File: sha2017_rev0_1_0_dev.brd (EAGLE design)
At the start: 95 x 86 mm, 196 parts, among them IC1 CP210X_USB_UART, IC2 AP7215, IC3 ESP32WROOM32, IC4 MCP73833, IC5 FXL6408, IC6 CPT112, Q1 MOSFET-PCHANNEL, Q2 MMBT2222A, Q3 MMBT2222A, Q4 MMBT2222A, Q5 MMBT2222A, Q6 SI1304 BDL, Q7 MMBT2222A, Q8 MOSFET-PCHANNEL, T1 SI2301DS, X1 2908-05WB-MG, X3 JST-PH3

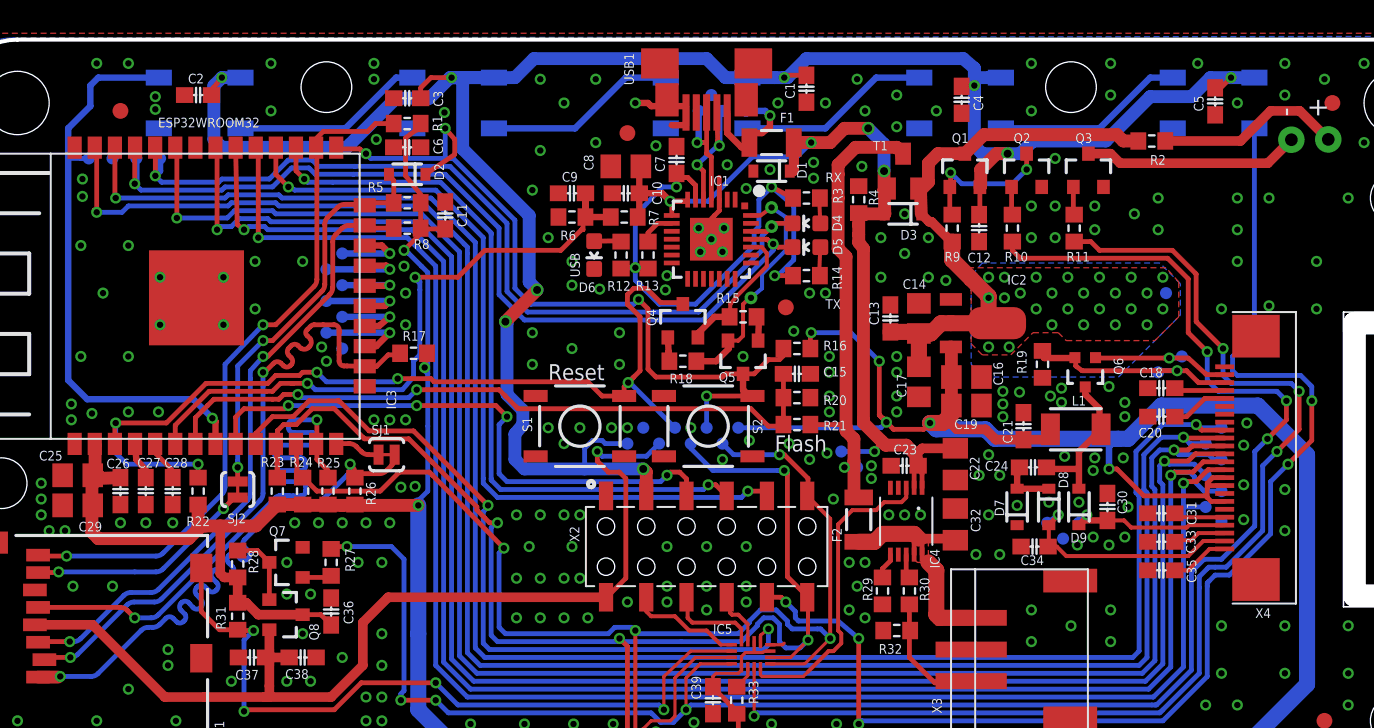
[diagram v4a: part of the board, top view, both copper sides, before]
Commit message: add 1 LED
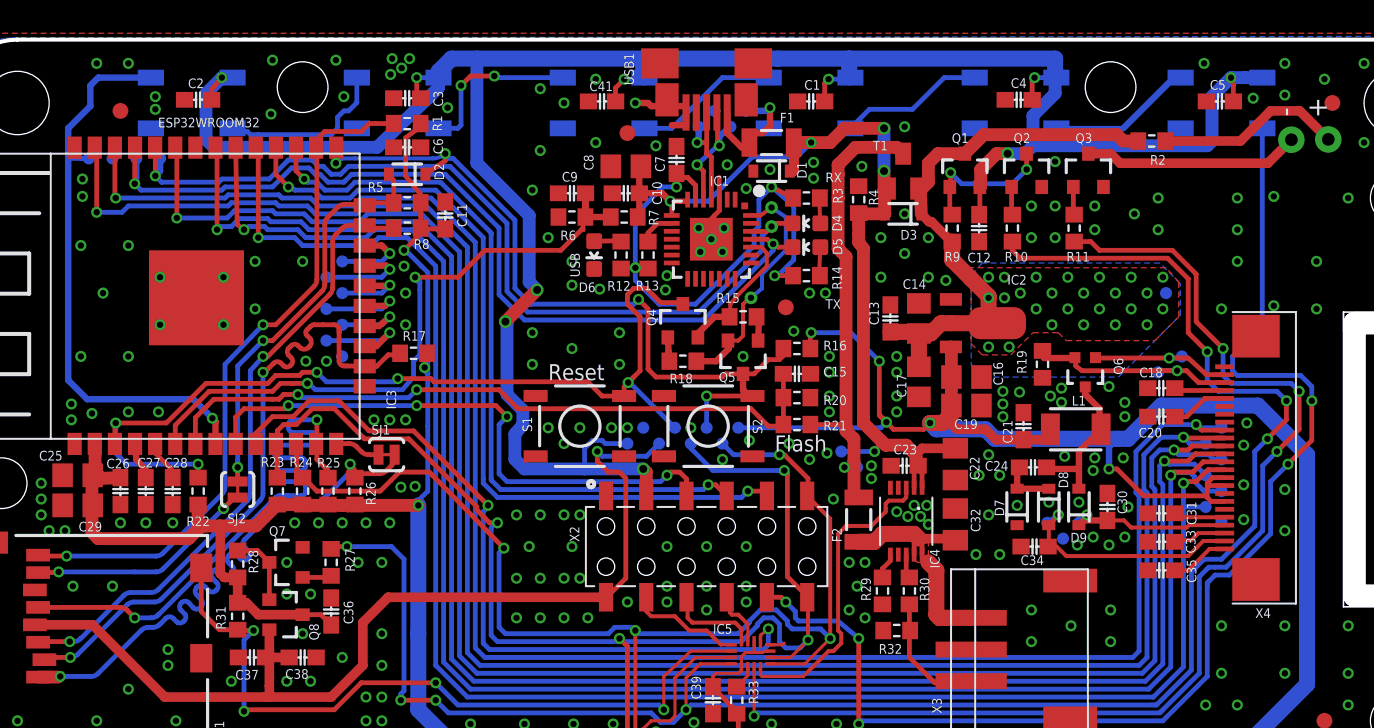
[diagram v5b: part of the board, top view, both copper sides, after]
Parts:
- added C41: 100n, sha2017_rev0_1_0_dev:C0603-DASHES
- added D105: (no value), SparkFun-LED:WS2812B
- moved D103 9.50 mm to (41.0, 81.0)
- moved D102 6.50 mm to (54.0, 81.0)
- moved C4 3.60 mm to (67.2, 81.2), turned to 180 degrees
- moved D101 3.50 mm to (67.0, 81.0)
- moved TP137 1.12 mm to (49.0, 79.5)
- moved TP139 1.02 mm to (48.0, 80.5)
- moved TP138 1.00 mm to (47.0, 79.5)
- moved C1 0.85 mm to (54.1, 81.1), turned to 0 degrees
- moved D100 0.50 mm to (80.0, 81.0)
- moved D104 0.50 mm to (15.0, 81.0)
- moved TP124 0.50 mm to (24.5, 65.0)
- moved TP125 0.50 mm to (23.5, 66.0)
- moved TP126 0.50 mm to (24.5, 67.0)
- moved TP127 0.50 mm to (23.5, 68.0)
- moved TP129 0.50 mm to (24.5, 69.0)
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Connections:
- removed net N$51: D103.4, D104.2
- new net N$3: D103.4, D105.2
- new net N$4: D104.2, D105.4
- net GND: now also C41.1, D105.3
- net WS2812_POWER: now also C41.2, D105.1
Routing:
- net N$51: track 12.2 -> 0.00 mm
- net N$4: track 0.00 -> 10.8 mm
- net N$3: track 0.00 -> 10.8 mm, vias 0 -> 2
- net WS2812_POWER: track 148.5 -> 153.9 mm, vias 9 -> 10
- net N$50: track 12.2 -> 9.17 mm
- net N$2: track 12.2 -> 9.17 mm
- net N$19: track 12.2 -> 9.17 mm
- net ESP32_FLASH: track 53.4 -> 50.6 mm
- net USB_DP_CON: track 8.30 -> 7.30 mm
- net USB_DN_CON: track 8.68 -> 7.87 mm
- net +5V: track 64.1 -> 64.7 mm
- net GND: vias 286 -> 282

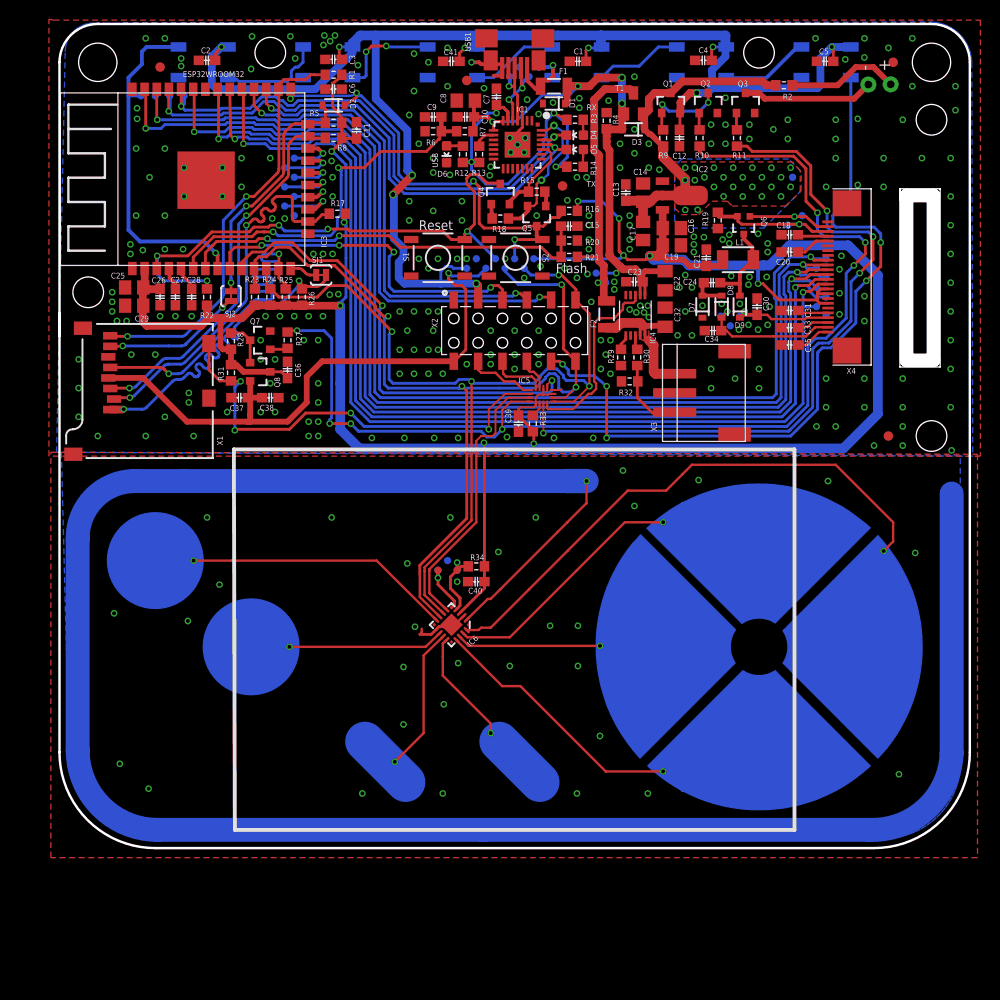
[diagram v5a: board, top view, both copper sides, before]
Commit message: adjusted values and add moe coper to the charger region
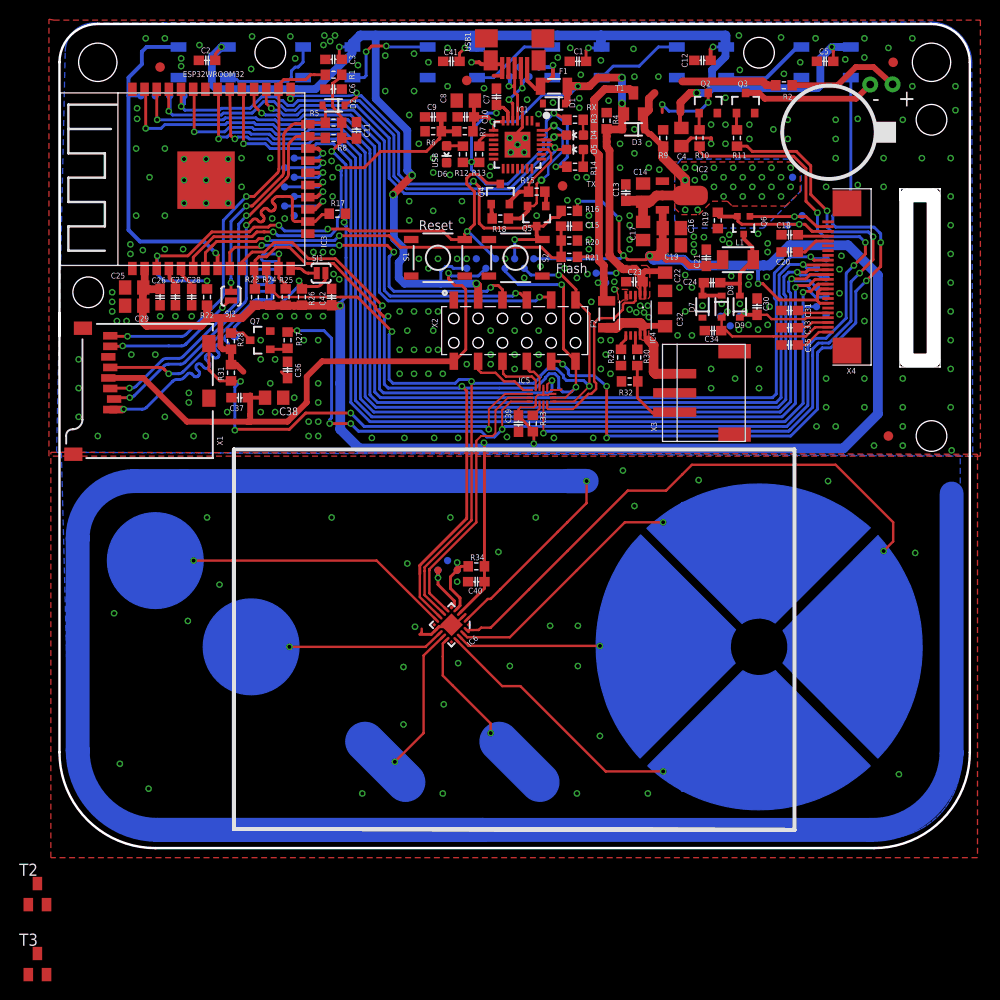
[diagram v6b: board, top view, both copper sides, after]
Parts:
- removed Q1, Q8: MOSFET-PCHANNEL, SparkFun-DiscreteSemi:SOT23-3
- added C42: 100n, sha2017_rev0_1_0_dev:C0603-DASHES
- added T2, T3: SI2301DS, transistor-small-signal:SOT23
- C22, C32: value 10u -> 4u7/16V; device rcl:C0805K -> rcl:C0805
- C38, C4: device 00ralf:C0603-DASHES -> rcl:C0805
- C39: value (none) -> 100n
- D100, D101, D102, D103, D104, D105: value (none) -> SK6812
- R2: value 10R -> 27R
- SJ1, SJ2: value JUMPER-PAD-2-NC_BY_TRACE -> JUMPER-PAD-2-NOYES_SILK; device SparkFun-Passives:PAD-JUMPER-2-NC_BY_TRACE_YES_SILK -> SparkFun-Passives:PAD-JUMPER-2-NO_YES_SILK
- moved C12 8.45 mm to (67.1, 81.2), turned to 0 degrees
- moved C4 8.32 mm to (64.9, 73.2), turned to 270 degrees
- moved C38 0.40 mm to (22.4, 46.0)
- moved SJ1 0.20 mm to (27.3, 59.0)
- moved U$1 0.20 mm to (80.5, 73.7)
- moved C22 0.10 mm to (63.2, 58.1), turned to 270 degrees
- turned C32 to 90 degrees
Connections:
- net +3V3: now also C42.1; no longer Q8.3
- net +5V: now also C22.1; no longer C22.2
- net 3V3_SWITCHED: no longer Q8.2
- net GND: now also C22.2, C32.2, C42.2; no longer C22.1, C32.1
- net N$17: now also T3.1; no longer Q8.1
- net N$49: now also C32.1; no longer C32.2
- net N$53: now also T2.1; no longer Q1.1
- net VCC: no longer Q1.3
- net WS2812_POWER: no longer Q1.2
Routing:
- net PROXIMITY: track 224.4 -> 258.4 mm
- net GND: track 15.0 -> 19.1 mm, vias 282 -> 301
- net +3V3: track 269.8 -> 266.3 mm
- net VCC: track 38.3 -> 34.9 mm
- net N$17: track 4.66 -> 2.31 mm
- net N$53: track 9.20 -> 7.52 mm
- net 3V3_SWITCHED: track 63.9 -> 62.8 mm
- net I2C_SCL: track 95.3 -> 94.3 mm
- net WS2812_POWER: track 153.9 -> 154.4 mm
- added copper zone on layer 1, net +5V
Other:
- board text added: "+"
- board text added: "-"

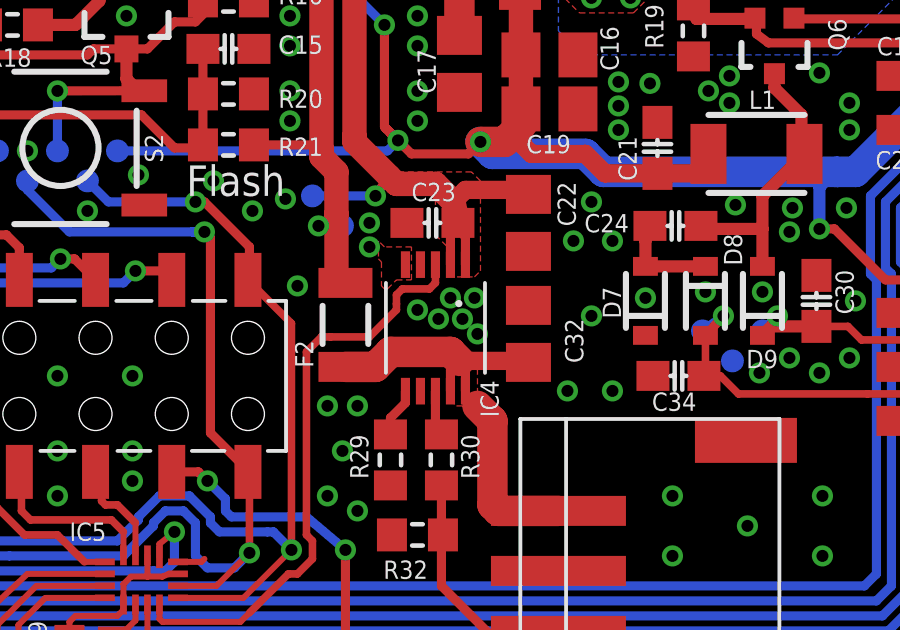
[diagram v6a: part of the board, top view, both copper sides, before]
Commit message: MOOOOOOOORRRRREEEEEEE VIAS for the charger
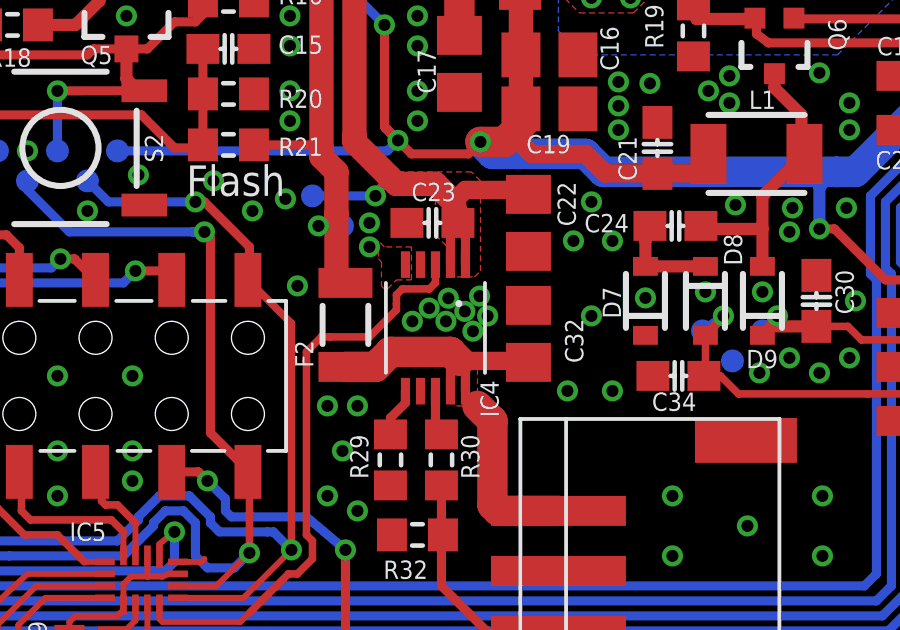
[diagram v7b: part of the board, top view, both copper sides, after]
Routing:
- net GND: vias 301 -> 303
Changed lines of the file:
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@@
 <setting verticaltext="up"/>
 </settings>
-<grid distance="0.1" unitdist="mm" unit="mm" style="lines" multiple="1" display="yes" altdistance="0.025" altunitdist="inch" altunit="inch"/>
+<grid distance="0.01" unitdist="mm" unit="mm" style="lines" multiple="1" display="yes" altdistance="0.025" altunitdist="inch" altunit="inch"/>
 <layers>
 <layer number="1" name="Top" color="4" fill="1" visible="yes" active="yes"/>
@@
 <via x="64.5" y="52.5" extent="1-16" drill="0.4"/>
 <via x="66" y="52.5" extent="1-16" drill="0.4"/>
-<via x="59.5" y="55.2" extent="1-16" drill="0.4"/>
-<via x="60.2" y="54.9" extent="1-16" drill="0.4"/>
-<via x="61" y="54.9" extent="1-16" drill="0.4"/>
+<via x="59.89" y="55.26" extent="1-16" drill="0.4"/>
+<via x="60.45" y="54.82" extent="1-16" drill="0.4"/>
+<via x="61.08" y="55.15" extent="1-16" drill="0.4"/>
 <via x="57.5" y="52" extent="1-16" drill="0.4"/>
 <via x="56.5" y="52" extent="1-16" drill="0.4"/>
@@
 <via x="81.4" y="56.9" extent="1-16" drill="0.4"/>
 <via x="81.4" y="59.4" extent="1-16" drill="0.4"/>
-<via x="60.6" y="55.6" extent="1-16" drill="0.4"/>
-<via x="61.4" y="55.6" extent="1-16" drill="0.4"/>
-<via x="61.5" y="54.4" extent="1-16" drill="0.4"/>
+<via x="60.53" y="55.59" extent="1-16" drill="0.4"/>
+<via x="61.57" y="55.66" extent="1-16" drill="0.4"/>
+<via x="61.84" y="55" extent="1-16" drill="0.4"/>
 <contactref element="D105" pad="3"/>
 <contactref element="C41" pad="1"/>
@@
 <vertex x="58.3" y="56"/>
 </polygon>
+<via x="59.33" y="54.82" extent="1-16" drill="0.4"/>
+<via x="61.35" y="54.49" extent="1-16" drill="0.4"/>
 </signal>
 <signal name="USB_DN_CON">

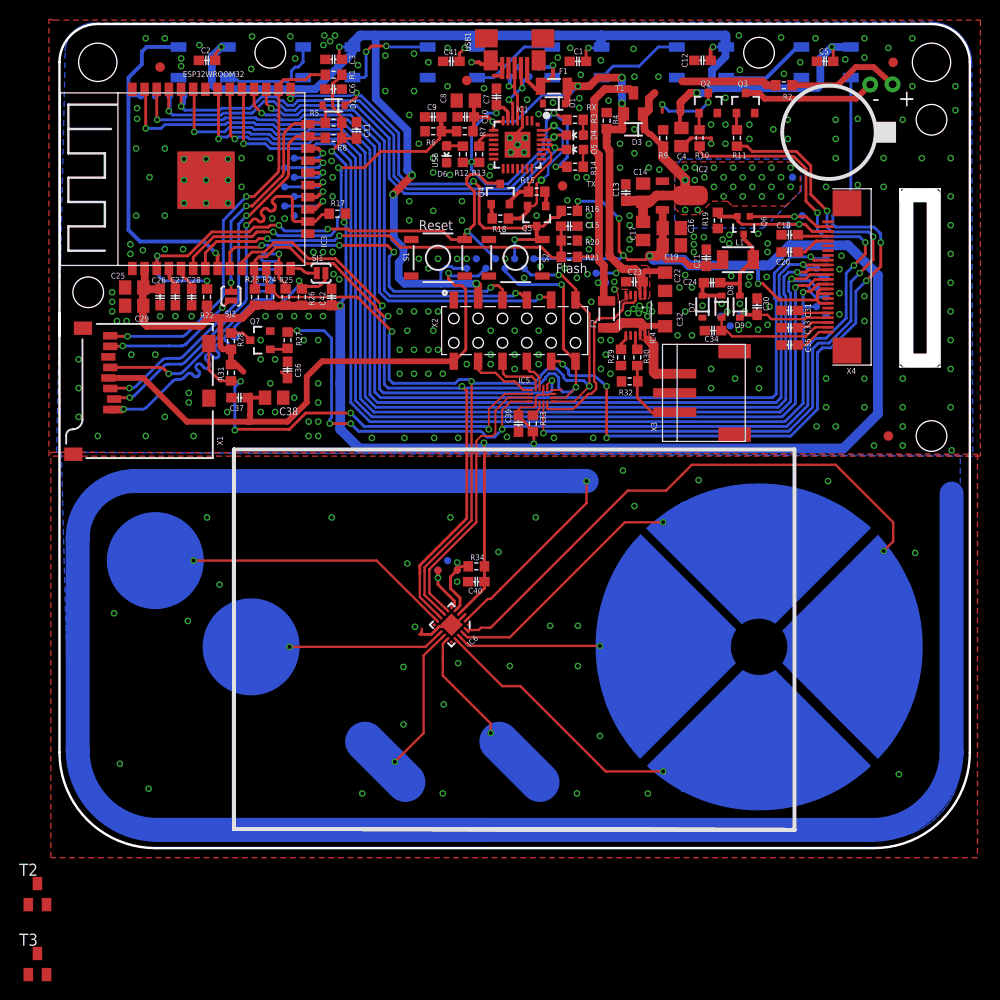
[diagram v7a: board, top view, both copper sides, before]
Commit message: fixed bug at powersupply Mosfets was N channel and need to be P channel to switch the Highside voltage
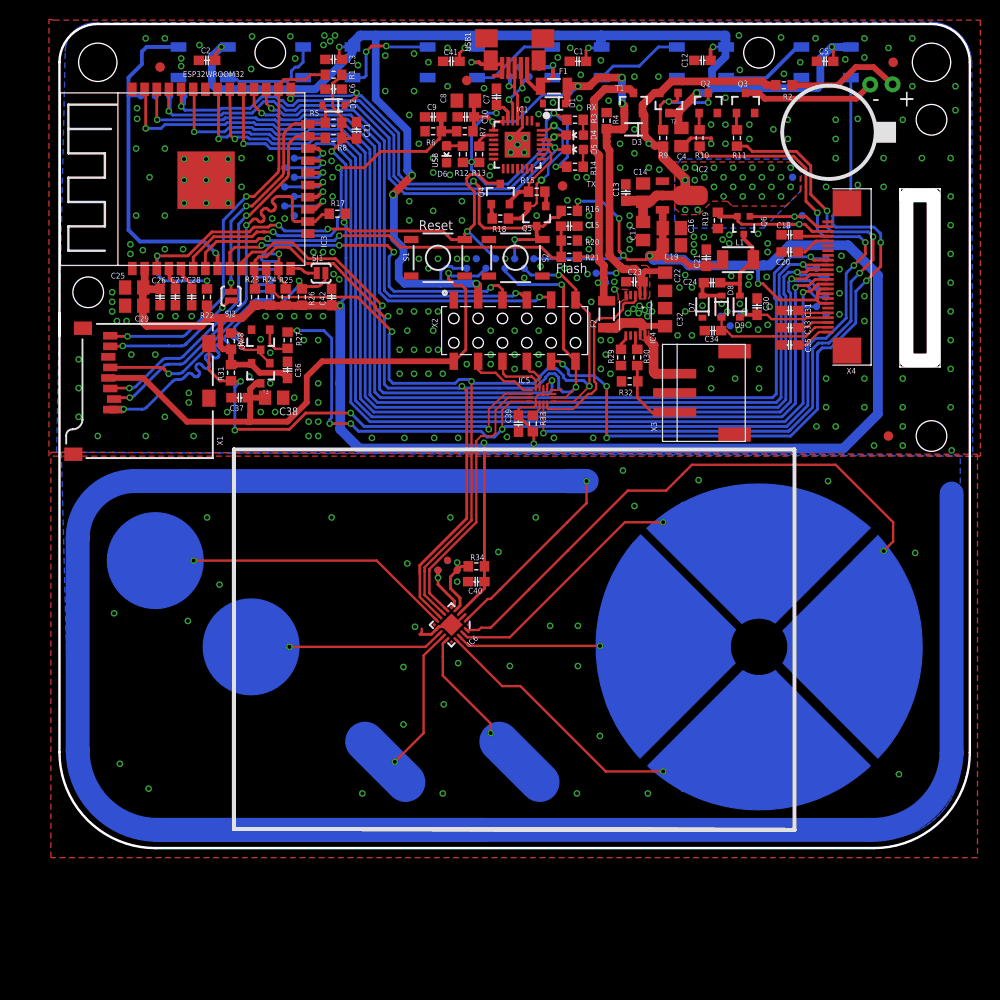
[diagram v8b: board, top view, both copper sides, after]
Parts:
- added TP3: TEST-POINT3, SparkFun-Passives:PAD.03X.03
- T1, T2, T3: device transistor-small-signal:SOT23 -> SparkFun-DiscreteSemi:SOT23-3
- moved T2 105.7 mm to (63.6, 76.8), turned to 180 degrees
- moved T3 66.0 mm to (21.0, 48.6), turned to 180 degrees
- moved Q7 0.10 mm to (21.0, 52.1), turned to 180 degrees
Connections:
- net +3V3: now also T3.2
- net 3V3_SWITCHED: now also T3.3
- net GND: now also TP3.P$1
- net VCC: now also T2.2
- net WS2812_POWER: now also T2.3
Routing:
- net +3V3: track 266.3 -> 270.4 mm
- net N$17: track 2.31 -> 6.32 mm
- net VCC: track 34.9 -> 38.7 mm
- net N$53: track 7.52 -> 10.8 mm
- net 3V3_SWITCHED: track 62.8 -> 65.1 mm
- net N$15: track 1.84 -> 3.69 mm
- net WS2812_POWER: track 154.4 -> 155.3 mm
